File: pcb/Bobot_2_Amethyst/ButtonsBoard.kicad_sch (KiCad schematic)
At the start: 2 parts

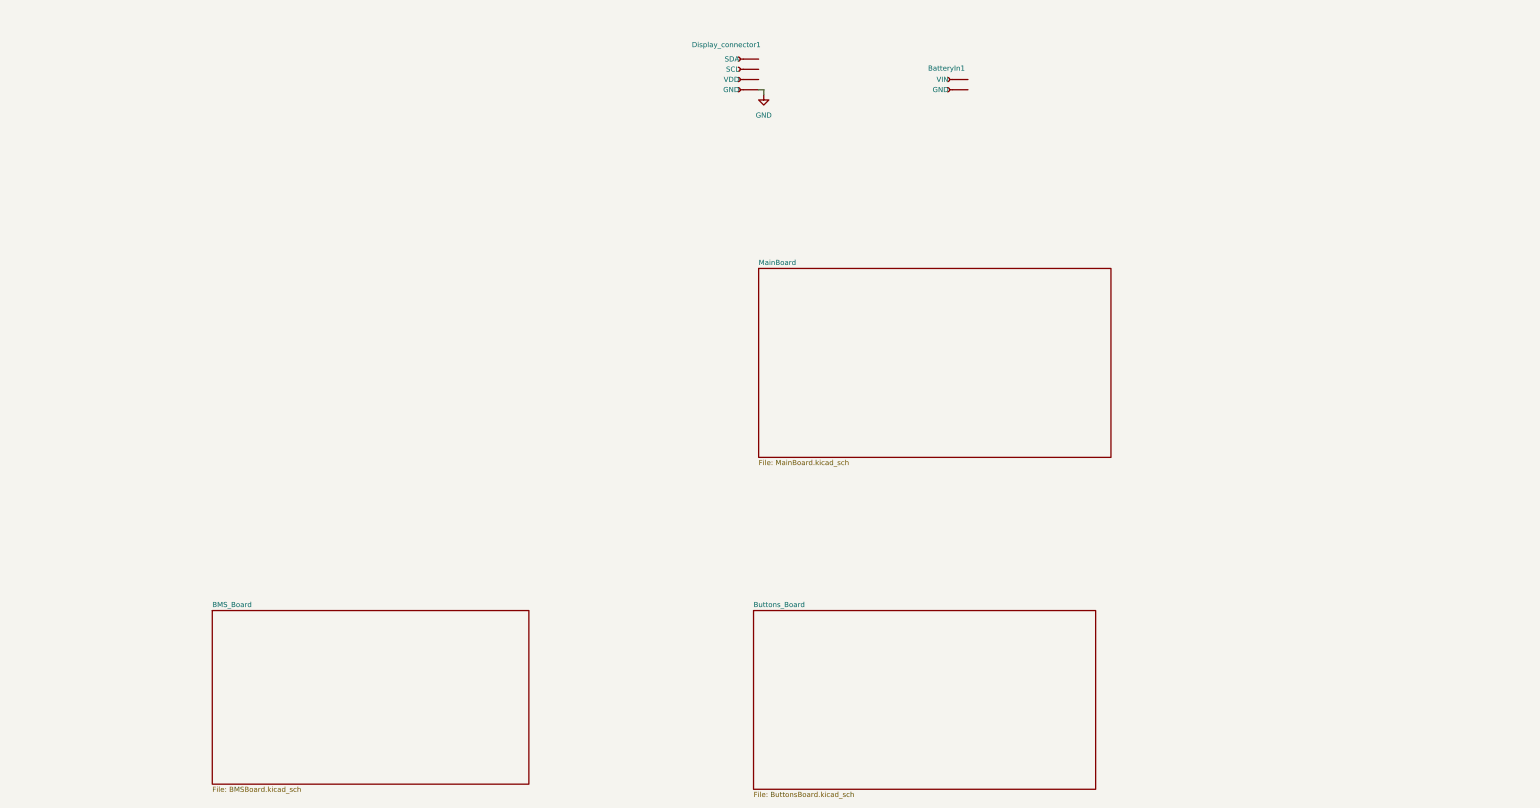
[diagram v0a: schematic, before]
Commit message: pcb: reorganize kicad project and add basic schematics
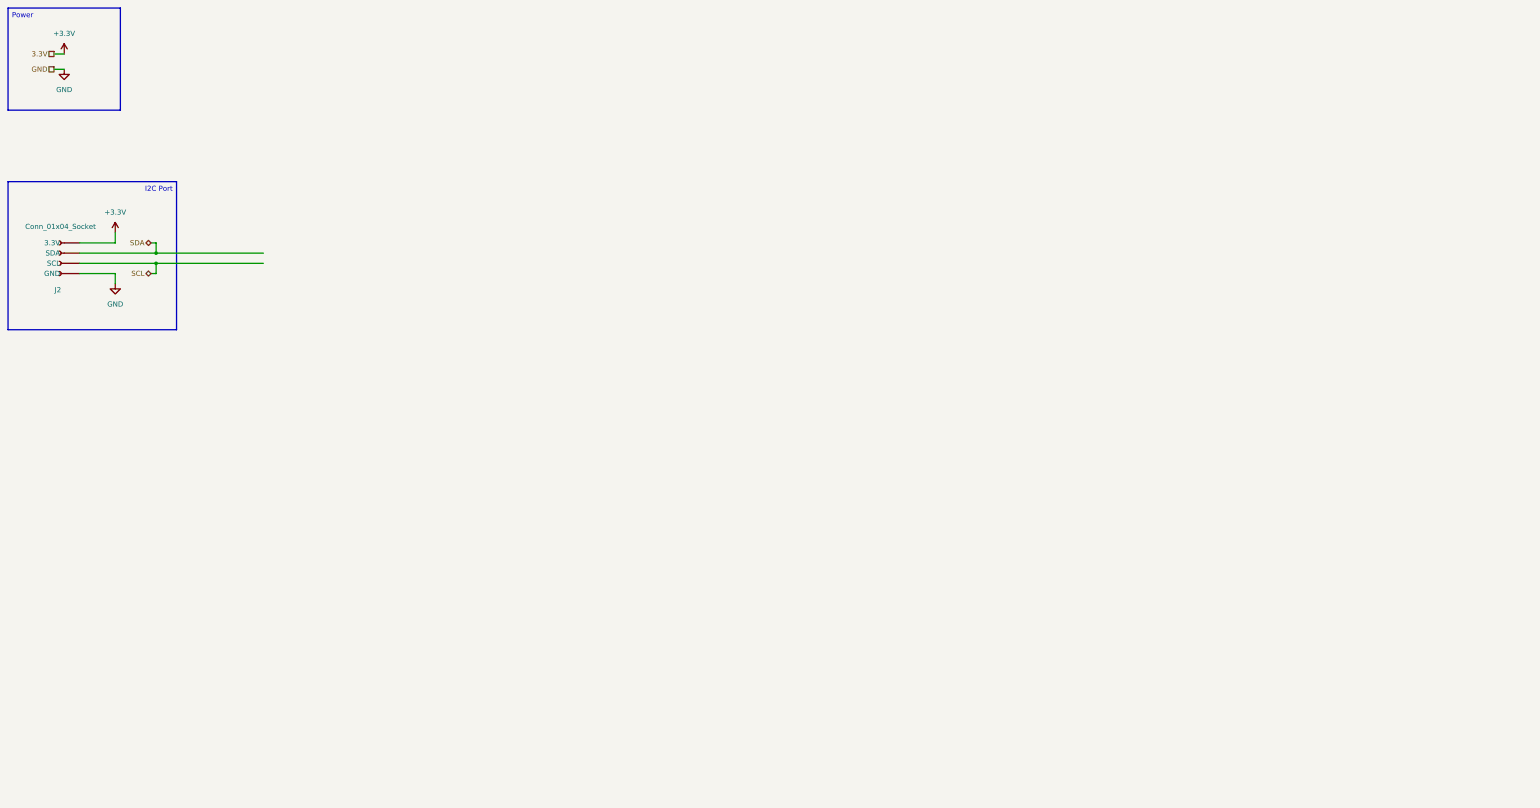
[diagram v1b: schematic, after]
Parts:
- removed BatteryIn1: Conn_01x02_Socket, Connector_JST:JST_XH_B2B-XH-A_1x02_P2.50mm_Vertical, symbol Connector:Conn_01x02_Socket
- removed Display_connector1: Conn_01x04_Socket, Connector_JST:JST_XH_B4B-XH-A_1x04_P2.50mm_Vertical, symbol Connector:Conn_01x04_Socket
- added J2: Conn_01x04_Socket, Connector_JST:JST_XH_B4B-XH-AM_1x04_P2.50mm_Vertical, symbol Connector:Conn_01x04_Socket
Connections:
- net GND: now also J2.4 (GND)
- new net +3.3V: J2.1 (3.3V)
- new net SCL: J2.3 (SCL)
- new net SDA: J2.2 (SDA)
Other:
- removed sheet BMS_Board
- removed sheet Buttons_Board
- removed sheet MainBoard

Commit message: pcb: add buttons board schematics except I2C address
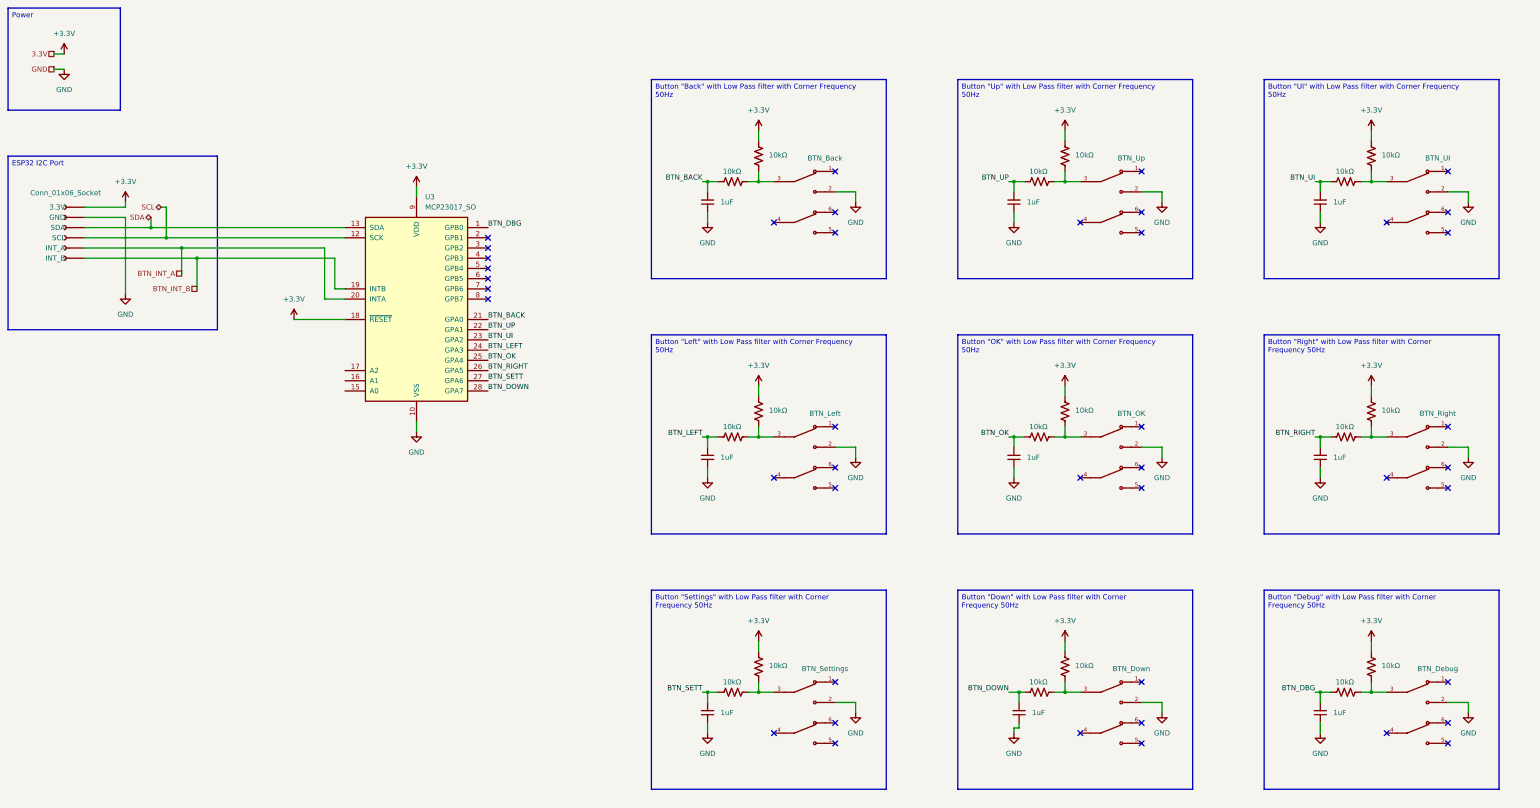
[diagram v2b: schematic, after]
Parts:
- removed J2: Conn_01x04_Socket, Connector_JST:JST_XH_B4B-XH-AM_1x04_P2.50mm_Vertical, symbol Connector:Conn_01x04_Socket
- added C10, C11, C12, C13, C14, C15, C16, C8, C9: 1uF, Capacitor_SMD:C_0805_2012Metric_Pad1.18x1.45mm_HandSolder, symbol Device:C_Small
- added J8: Conn_01x06_Socket, Connector_JST:JST_XH_B6B-XH-A_1x06_P2.50mm_Vertical, symbol Connector:Conn_01x06_Socket
- added R10, R11, R12, R13, R14, R15, R16, R17, R18, R19, R20, R21, R22, R23, R6, R7, R8, R9: 10kΩ, Resistor_SMD:R_0805_2012Metric_Pad1.20x1.40mm_HandSolder, symbol Device:R_US
- added S1: BTN_Back, TL2285OA:SW_TL2285OA, symbol TL2285OA:TL2285OA
- added S2: BTN_Up, TL2285OA:SW_TL2285OA, symbol TL2285OA:TL2285OA
- added S3: BTN_UI, TL2285OA:SW_TL2285OA, symbol TL2285OA:TL2285OA
- added S4: BTN_Left, TL2285OA:SW_TL2285OA, symbol TL2285OA:TL2285OA
- added S5: BTN_OK, TL2285OA:SW_TL2285OA, symbol TL2285OA:TL2285OA
- added S6: BTN_Right, TL2285OA:SW_TL2285OA, symbol TL2285OA:TL2285OA
- added S7: BTN_Settings, TL2285OA:SW_TL2285OA, symbol TL2285OA:TL2285OA
- added S8: BTN_Down, TL2285OA:SW_TL2285OA, symbol TL2285OA:TL2285OA
- added S9: BTN_Debug, TL2285OA:SW_TL2285OA, symbol TL2285OA:TL2285OA
- added U3: MCP23017_SO, Package_SO:SOIC-28W_7.5x17.9mm_P1.27mm, symbol Interface_Expansion:MCP23017_SO
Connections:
- net +3.3V: now also J8.1 (3.3V), R11.2, R13.2, R15.2, R17.2, R19.2, R21.2, R23.2, R6.2, R9.2, U3.18 (~{RESET}), U3.9 (VDD)
- net GND: now also C10.1, C11.1, C12.1, C13.1, C14.1, C15.1, C16.1, C8.1, C9.1, J8.2 (GND), S1.2, S2.2, S3.2, S4.2, S5.2, S6.2, S7.2, S8.2, S9.2, U3.10 (VSS)
- net SCL: now also J8.4 (SCL), U3.12 (SCK)
- net SDA: now also J8.3 (SDA), U3.13 (SDA)
- new net: R14.1, R15.1, S5.3
- new net: R18.1, R19.1, S7.3
- new net: R12.1, R13.1, S4.3
- new net: R20.1, R21.1, S8.3
- new net: R6.1, R7.1, S1.3
- new net: R16.1, R17.1, S6.3
- new net: R10.1, R11.1, S3.3
- new net: R22.1, R23.1, S9.3
- new net: R8.1, R9.1, S2.3
- new net BTN_BACK: C8.2, R7.2, U3.21 (GPA0)
- new net BTN_DBG: C16.2, R22.2, U3.1 (GPB0)
- new net BTN_DOWN: C15.2, R20.2, U3.28 (GPA7)
- new net BTN_INT_A: J8.5 (INT_A), U3.20 (INTA)
- new net BTN_INT_B: J8.6 (INT_B), U3.19 (INTB)
- new net BTN_LEFT: C11.2, R12.2, U3.24 (GPA3)
- new net BTN_OK: C12.2, R14.2, U3.25 (GPA4)
- new net BTN_RIGHT: C13.2, R16.2, U3.26 (GPA5)
- new net BTN_SETT: C14.2, R18.2, U3.27 (GPA6)
- new net BTN_UI: C10.2, R10.2, U3.23 (GPA2)
- new net BTN_UP: C9.2, R8.2, U3.22 (GPA1)
- no-connect marks 0 -> 43

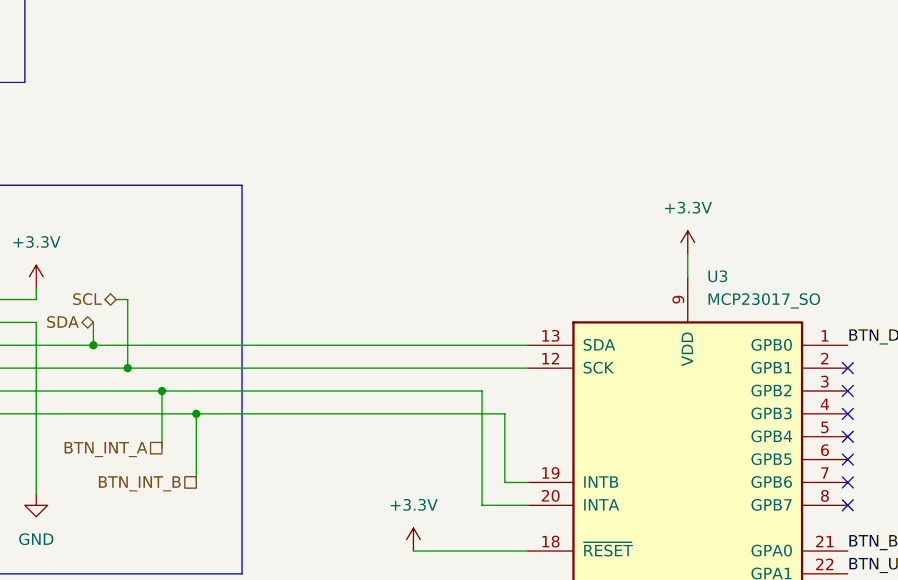
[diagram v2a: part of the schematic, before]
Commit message: pcb: add touch sensor board
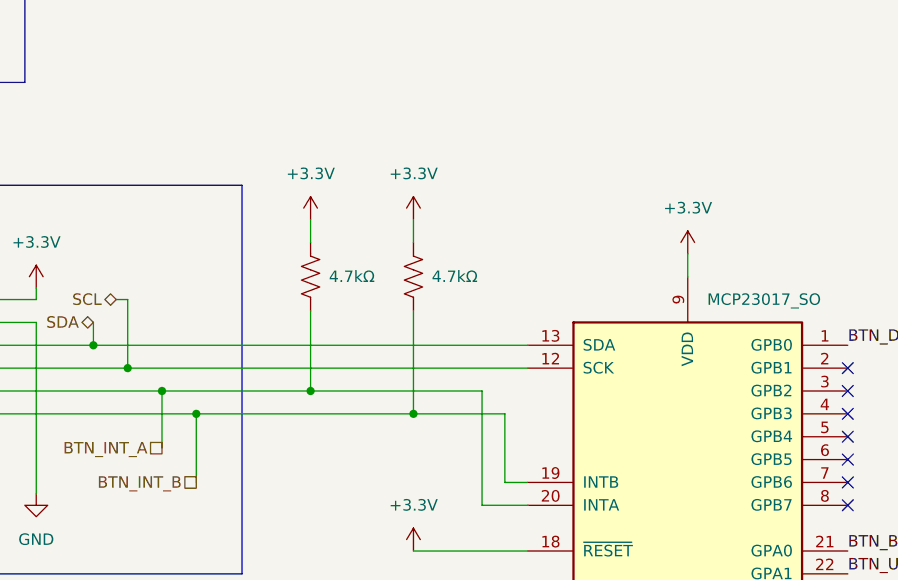
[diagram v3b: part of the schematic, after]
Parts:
- added R26, R27: 4.7kΩ, Resistor_SMD:R_0805_2012Metric_Pad1.20x1.40mm_HandSolder, symbol Device:R_US
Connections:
- net +3.3V: now also R26.1, R27.1
- net BTN_INT_A: now also R26.2
- net BTN_INT_B: now also R27.2
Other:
- title: (none) -> Buttons Board with MCP23017_SO
